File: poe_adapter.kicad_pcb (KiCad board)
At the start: 2 copper layers, 170 parts, among them J1 USB_C_Receptacle, J2 RJ45_LED_Shielded, J6 Conn_01x02, J7 Conn_01x03_Male, Q1 BSC118N10NSG, Q2 BSC118N10NSG, Q3 AO3409, Q4 AO3401A, Q5 AO3401A, U1 LM2575HVS, U2 LAN7800/Y9X, U3 93AA66C, U4 FDMQ8205A, U5 FDMQ8205A, U6 TPS2372-4RGWR, U7 LM5116, U8 STUSB4700, Y1 25MHz

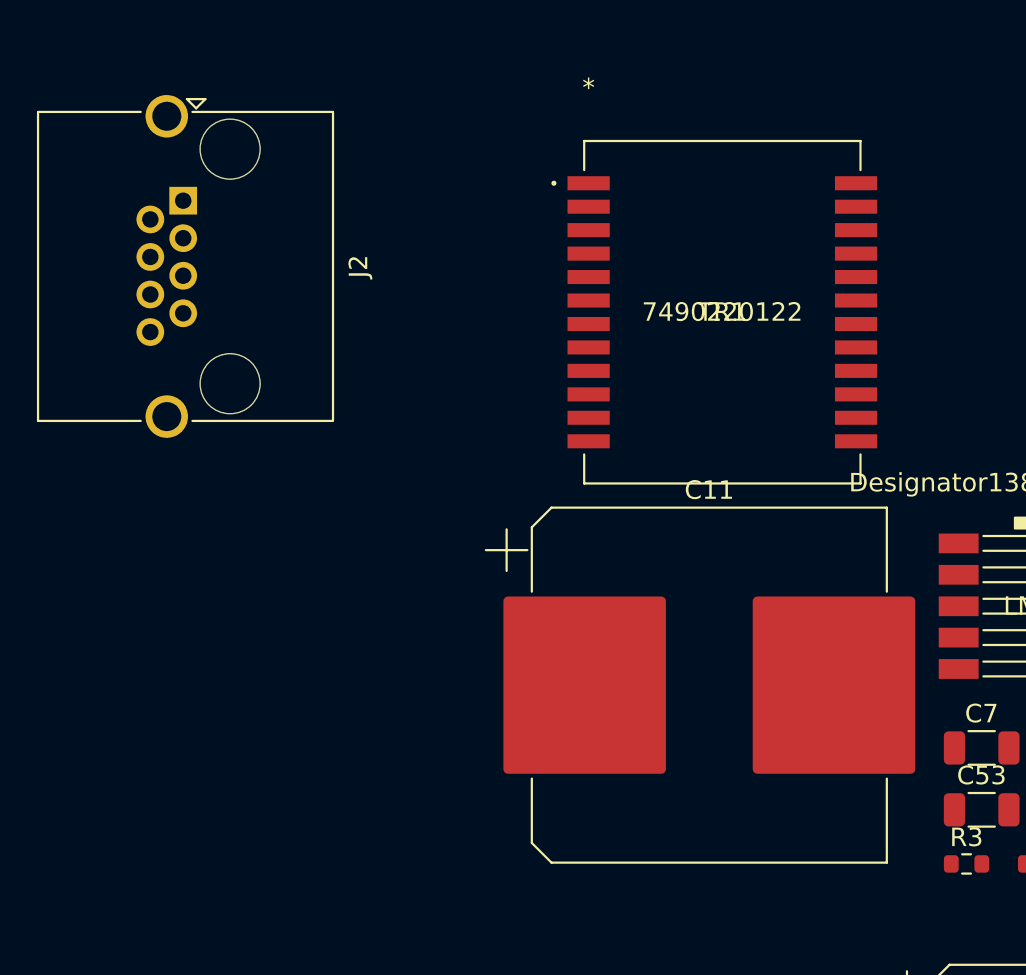
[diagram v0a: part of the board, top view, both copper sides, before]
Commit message: PCB Design Rule updated
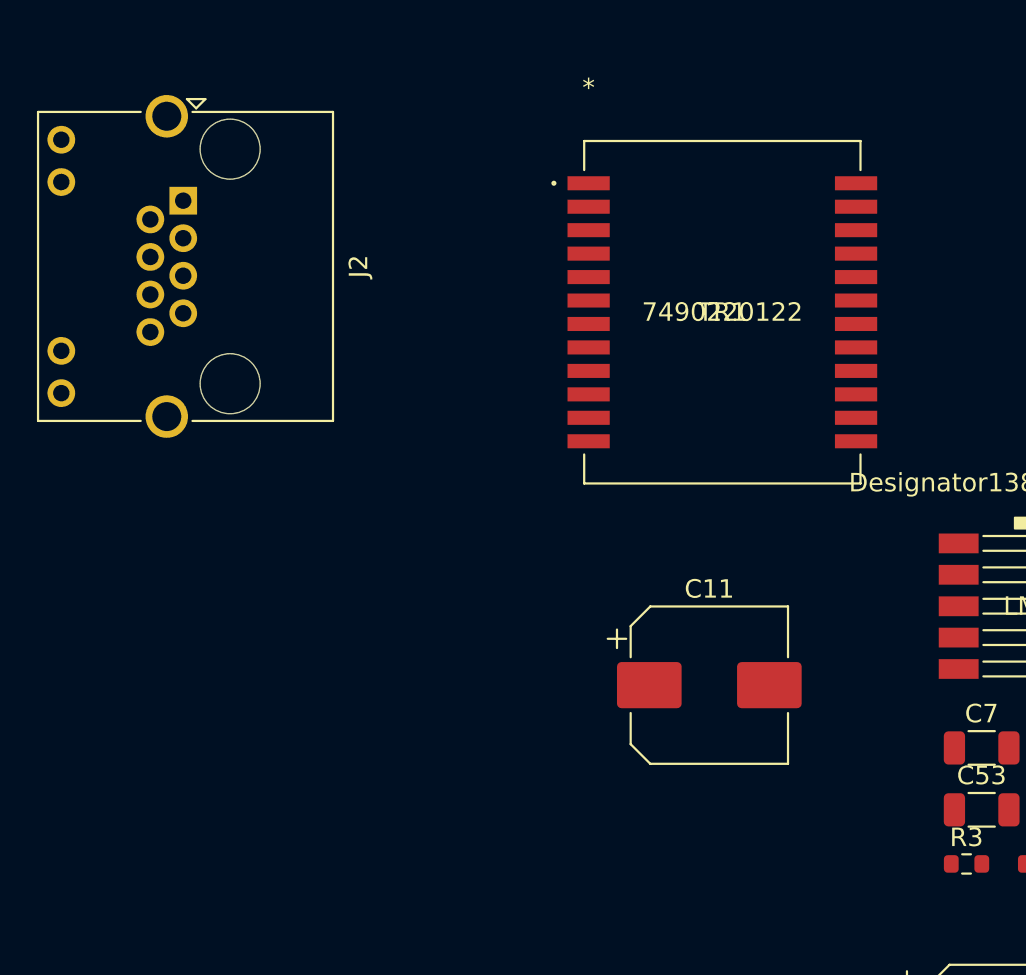
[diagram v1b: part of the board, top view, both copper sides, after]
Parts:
- C11: footprint Capacitor_SMD:CP_Elec_18x17.5 -> Capacitor_SMD:CP_Elec_8x10
- J2: footprint Connector_RJ:RJ45_Amphenol_RJHSE5380 -> Connector_RJ:RJ45_Amphenol_RJHSE538X
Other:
- copper layers 2 -> 4

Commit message: Layout Update
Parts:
- moved C15 83.6 mm to (129.5, 40.6)
- moved C16 83.6 mm to (129.5, 45.7)
- moved TP3 83.6 mm to (133.1, 46.5)
- moved C13 83.6 mm to (129.5, 38.1)
- moved C14 83.6 mm to (137.6, 36.2)
- moved C18 83.6 mm to (129.5, 35.6)
- moved C19 83.6 mm to (121.2, 48.0)
- moved C20 83.6 mm to (125.2, 48.0)
- moved C21 83.6 mm to (133.6, 40.6)
- moved L2 83.6 mm to (126.4, 31.6)
- moved R13 83.6 mm to (125.5, 39.6)
- moved R14 83.6 mm to (125.5, 44.7)
- moved R15 83.6 mm to (129.5, 43.1)
- moved R8 83.6 mm to (121.2, 50.5)
- moved R9 83.6 mm to (117.2, 50.5)
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
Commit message: crude layout
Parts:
- moved C35 90.4 mm to (273.7, 133.1)
- moved C37 90.4 mm to (276.2, 123.1)
- moved C42 90.4 mm to (273.7, 130.6)
- moved C45 90.4 mm to (273.7, 128.1)
- moved R38 90.4 mm to (288.6, 117.5)
- moved R48 90.4 mm to (272.4, 120.3)
- moved C40 90.4 mm to (277.7, 128.1)
- moved C41 90.4 mm to (280.2, 122.3)
- moved C48 90.4 mm to (275.9, 125.6)
- moved C49 90.4 mm to (251.3, 129.2)
- moved D6 90.4 mm to (261.2, 131.8)
- moved D7 90.4 mm to (267.5, 125.5)
- moved L4 90.4 mm to (253.8, 147.0)
- moved R35 90.4 mm to (271.9, 125.6)
- moved R44 90.4 mm to (276.6, 119.8)
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
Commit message: layout power stage
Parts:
- moved C36 89.1 mm to (194.8, 155.3), turned to 90 degrees
- moved R39 87.7 mm to (198.8, 151.4), turned to -90 degrees
- moved C41 86.9 mm to (196.5, 145.7), turned to -90 degrees
- moved C47 85.5 mm to (201.0, 138.3), turned to 180 degrees
- moved C48 85.2 mm to (190.8, 129.3)
- moved C38 84.5 mm to (191.8, 142.6)
- moved C31 83.7 mm to (224.0, 154.4), turned to 180 degrees
- moved C45 83.2 mm to (219.5, 64.9)
- moved C51 83.2 mm to (204.6, 45.5)
- moved J7 83.2 mm to (189.7, 53.6)
- moved Q4 83.2 mm to (207.5, 39.5)
- moved R24 83.2 mm to (216.9, 43.6)
- moved R34 83.2 mm to (203.2, 48.6)
- moved R38 83.2 mm to (234.4, 54.4)
- moved R52 83.2 mm to (223.5, 67.4)
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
